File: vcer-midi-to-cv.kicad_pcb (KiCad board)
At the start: 4 copper layers, 210.7 x 128.5 mm, 87 parts, among them J1 Conn_01x10_Male, J10 CV3, J11 CV4, J12 Vel1, J13 Vel2, J14 Vel3, J15 Vel4, J16 Gate1, J17 Gate2, J18 Gate3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

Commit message: I have some changes, but no idea what
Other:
- board size 210.7 x 128.5 mm -> 140 x 100 mm
- board text removed: "!!! TAKE COVER PANEL FROM THE VERSION 4 !!!"
- board text removed: "CV"
- board text removed: "Con"
- board text removed: "Data"
- board text removed: "Gate"
- board text removed: "I"
- board text removed: "II"
- board text removed: "III"
- board text removed: "IV"
- board text removed: "Pwr"
- board text removed: "USB"
- board text removed: "Upgrade"
- board text removed: "Vel"
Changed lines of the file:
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@@
   (gr_circle locked (center 9.01 95.96) (end 9.428688 95.96) (layer "B.SilkS") (width 0.15) (fill solid))
   (gr_circle (center 107.22 66.96) (end 107.638688 66.96) (layer "B.SilkS") (width 0.15) (fill solid))
-  (gr_line (start -79.99 -20.4) (end -9.72 -20.24) (layer "B.SilkS") (width 0.15))
-  (gr_line (start -80.49 119.63) (end -9.56 119.3) (layer "B.SilkS") (width 0.15))
   (gr_circle (center 136.4 23.94) (end 136.818688 23.94) (layer "B.SilkS") (width 0.15) (fill solid))
   (gr_circle (center 124.87 66.36) (end 125.288688 66.36) (layer "B.SilkS") (width 0.15) (fill solid))
-  (gr_line (start -9.72 119.97) (end -79.99 -20.4) (layer "B.SilkS") (width 0.15))
   (gr_circle locked (center 9.02 4.23) (end 9.438688 4.23) (layer "B.SilkS") (width 0.15) (fill solid))
   (gr_circle (center 104.31 51.66) (end 104.728688 51.66) (layer "B.SilkS") (width 0.15) (fill solid))
   (gr_circle (center 137.76 67.79) (end 138.178688 67.79) (layer "B.SilkS") (width 0.15) (fill solid))
-  (gr_line (start -9.72 -20.24) (end -80.49 119.63) (layer "B.SilkS") (width 0.15))
   (gr_circle (center 108 4.211312) (end 108.418688 4.211312) (layer "F.SilkS") (width 0.15) (fill solid))
   (gr_circle (center 115.4 66.08) (end 115.818688 66.08) (layer "F.SilkS") (width 0.15) (fill solid))
@@
   (gr_circle (center 108.68 95.29) (end 109.098688 95.29) (layer "F.SilkS") (width 0.15) (fill solid))
   (gr_circle (center 132.7 66.22) (end 133.118688 66.22) (layer "F.SilkS") (width 0.15) (fill solid))
-  (gr_line (start -20.194086 -14.25) (end -20.194086 114.25) (layer "Edge.Cuts") (width 0.15))
-  (gr_line (start -70.694086 114.25) (end -20.194086 114.25) (layer "Edge.Cuts") (width 0.15))
-  (gr_line (start -70.694086 -14.25) (end -20.194086 -14.25) (layer "Edge.Cuts") (width 0.15))
+  (gr_line locked (start 40 100) (end 40 0) (layer "Edge.Cuts") (width 0.2))
+  (gr_line locked (start 0 100) (end 0 0) (layer "Edge.Cuts") (width 0.2))
+  (gr_line locked (start 0 100) (end 40 100) (layer "Edge.Cuts") (width 0.2))
+  (gr_line locked (start 140 100) (end 140 0) (layer "Edge.Cuts") (width 0.2))
+  (gr_line locked (start 0 0) (end 40 0) (layer "Edge.Cuts") (width 0.2))
+  (gr_line locked (start 100 100) (end 100 0) (layer "Edge.Cuts") (width 0.2))
+  (gr_line locked (start 100 0) (end 140 0) (layer "Edge.Cuts") (width 0.2))
   (gr_line locked (start 100 100) (end 140 100) (layer "Edge.Cuts") (width 0.2))
-  (gr_line locked (start 0 100) (end 0 0) (layer "Edge.Cuts") (width 0.2))
-  (gr_line locked (start 140 100) (end 140 0) (layer "Edge.Cuts") (width 0.2))
-  (gr_line locked (start 0 100) (end 40 100) (layer "Edge.Cuts") (width 0.2))
-  (gr_line locked (start 40 100) (end 40 0) (layer "Edge.Cuts") (width 0.2))
-  (gr_line locked (start 100 0) (end 140 0) (layer "Edge.Cuts") (width 0.2))
-  (gr_line locked (start 0 0) (end 40 0) (layer "Edge.Cuts") (width 0.2))
-  (gr_line (start -70.694086 -14.25) (end -70.694086 114.25) (layer "Edge.Cuts") (width 0.15))
-  (gr_line locked (start 100 100) (end 100 0) (layer "Edge.Cuts") (width 0.2))
-  (gr_line (start -70.694086 -11.25) (end -20.194086 -11.25) (layer "User.8") (width 0.15))
   (gr_line locked (start 140 2.5) (end 100 2.5) (layer "User.8") (width 0.15))
   (gr_line locked (start 102.475 0.05) (end 102.475 100.05) (layer "User.8") (width 0.15))
   (gr_line locked (start 137.475 100.05) (end 137.475 0.05) (layer "User.8") (width 0.15))
-  (gr_line (start -70.694086 111.25) (end -20.194086 111.25) (layer "User.8") (width 0.15))
   (gr_line locked (start 40 99.5) (end 0 99.5) (layer "User.9") (width 0.15))
   (gr_line locked (start 100.5 100) (end 100.5 0) (layer "User.9") (width 0.15))
@@
     (effects (font (size 0.5 0.5) (thickness 0.125)) (justify mirror))
   )
-  (gr_text "III" (at -65.669086 69.775) (layer "F.SilkS")
-    (effects (font (size 2 2) (thickness 0.3)))
-  )
-  (gr_text "Pwr" (at -30.619086 16.2) (layer "F.SilkS")
-    (effects (font (size 1 1) (thickness 0.15)))
-  )
-  (gr_text "Data" (at -36.644086 16.2) (layer "F.SilkS")
-    (effects (font (size 1 1) (thickness 0.15)))
-  )
-  (gr_text "II" (at -65.669086 55.375) (layer "F.SilkS")
-    (effects (font (size 2 2) (thickness 0.3)))
-  )
-  (gr_text "Vel" (at -31.719086 34.525) (layer "F.SilkS")
-    (effects (font (size 2 2) (thickness 0.3)))
-  )
-  (gr_text "IV" (at -65.669086 84.175) (layer "F.SilkS")
-    (effects (font (size 2 2) (thickness 0.3)))
-  )
-  (gr_text "I" (at -65.669086 40.975) (layer "F.SilkS")
-    (effects (font (size 2 2) (thickness 0.3)))
-  )
-  (gr_text "Con" (at -42.819086 16.2) (layer "F.SilkS")
-    (effects (font (size 1 1) (thickness 0.15)))
-  )
   (gr_text "Back Panel" (at 107 3) (layer "F.SilkS")
     (effects (font (size 1 1) (thickness 0.15)))
@@
   (gr_text "Front Panel" (at 7 3) (layer "F.SilkS")
     (effects (font (size 1 1) (thickness 0.15)))
-  )
-  (gr_text "CV" (at -58.369086 34.525) (layer "F.SilkS")
-    (effects (font (size 2 2) (thickness 0.3)))
-  )
-  (gr_text "Gate" (at -45.294086 34.525) (layer "F.SilkS")
-    (effects (font (size 2 2) (thickness 0.3)))
-  )
-  (gr_text "USB" (at -53.744086 12.025) (layer "F.SilkS")
-    (effects (font (size 1 1) (thickness 0.15)))
-  )
-  (gr_text "Upgrade" (at -55.044086 27.775) (layer "F.SilkS")
-    (effects (font (size 1 1) (thickness 0.15)))
-  )
-  (gr_text "!!! TAKE COVER PANEL FROM THE VERSION 4 !!!" (at -44.93 56.53 45) (layer "User.4")
-    (effects (font (size 2 2) (thickness 0.15)))
   )
   (segment locked (start 112.525 30.779289) (end 112.525 29.875) (width 0.25) (layer "F.Cu") (net 1))
@@
     )
   )
-  (group "" (id 0d5502a4-78ea-4afd-9163-5fff06168194)
-    (members
-      0f01468d-4793-40a9-aa18-d4ec9b5eefff
-      30bb5606-9eda-48c1-9bd4-a93423426ac8
-      347abbc1-854a-40f3-be93-e7f380c88c8b
-      40dfc13f-f9a8-4ff3-bcab-1084fdf596c9
-      b5f8a962-6395-475e-a632-f26449ff4189
-      de954fc5-54aa-4912-850f-059c315d7062
-    )
-  )
   (group "" locked (id 3739076a-baeb-4668-95d4-28b7b5f3ab71)
     (members
@@
     )
   )
-  (group "" (id d4f87279-b883-4cb1-a4a4-84fef4bb4711)
-    (members
-      067063ef-affc-4d22-8463-eb3e4abccdc8
-      0d5502a4-78ea-4afd-9163-5fff06168194
-      2105cf5c-9eed-41f6-a88b-9d9562cde9a4
-      266e3bba-095d-4c7e-a334-d2acc8c5dfc8
-      34eb0245-4c12-4186-b799-98f2fe22efa8
-      3d3b04f2-b9f9-43bb-8d5b-593d5fcc3cf6
-      4c12a19f-f97f-45c8-8cfd-4d705aa2b9e7
-      51a33ff5-e59d-449b-875a-042da405201c
-      575d4f8c-99b7-4588-a1dd-31e4d0008428
-      94325249-10dc-49aa-b4bc-3f8b4aee802f
-      9b229dce-e01f-436d-aa19-067b1fc2c250
-      c69a4a08-fb84-4571-9982-802ea557f9b2
-      d39554fa-e09b-403f-be3b-055b6f2061d2
-    )
-  )

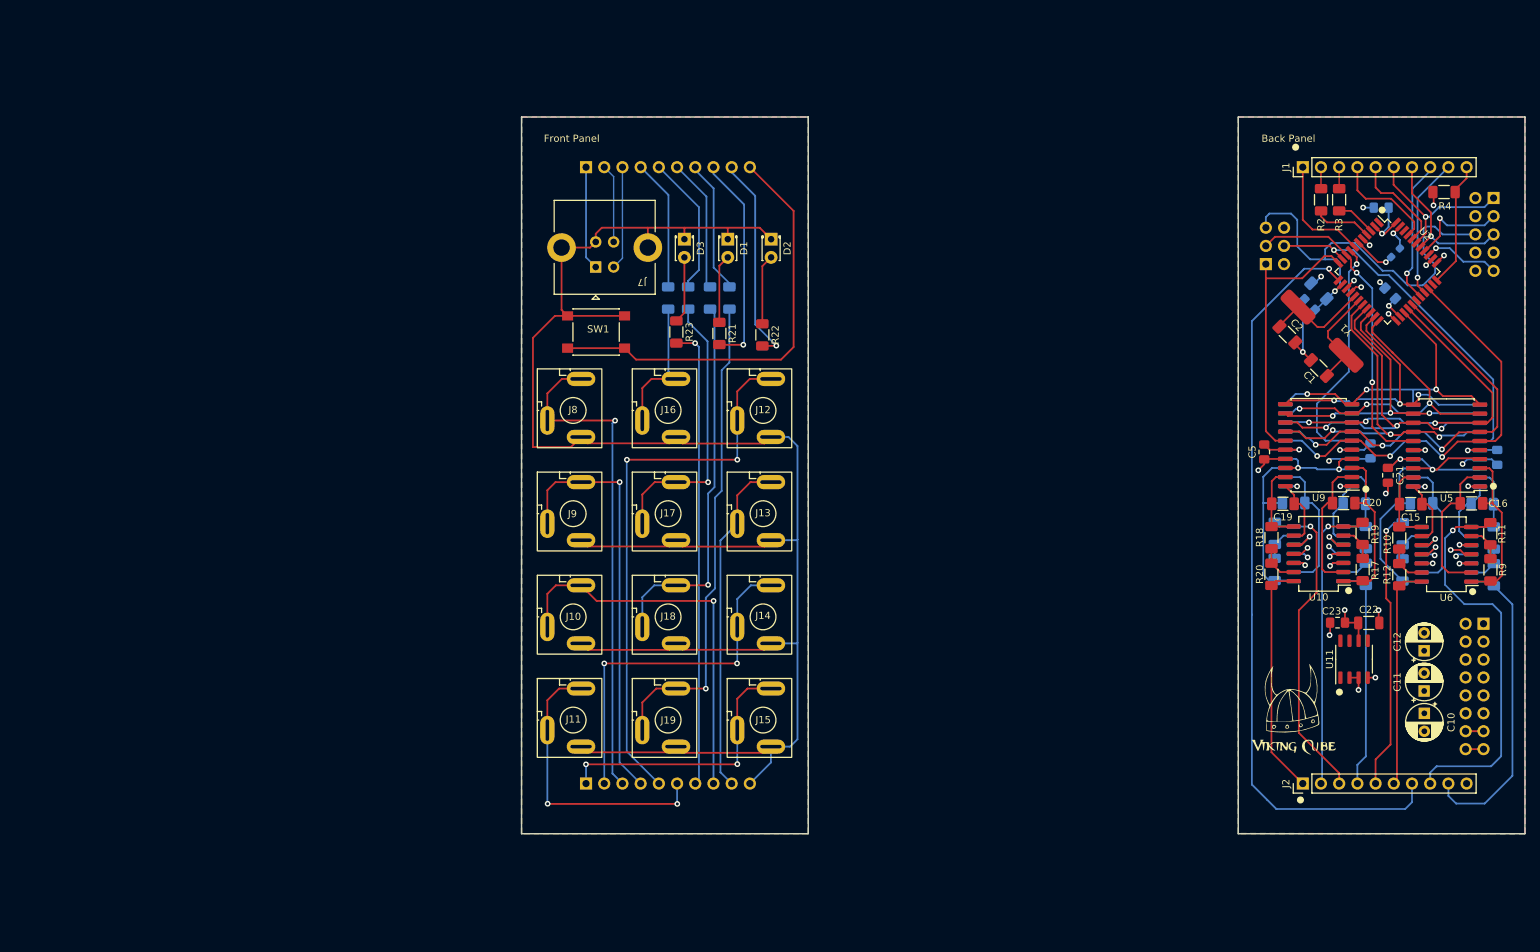
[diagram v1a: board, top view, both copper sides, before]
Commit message: recovered the cover plate from the old version - I declare v2.0 here by
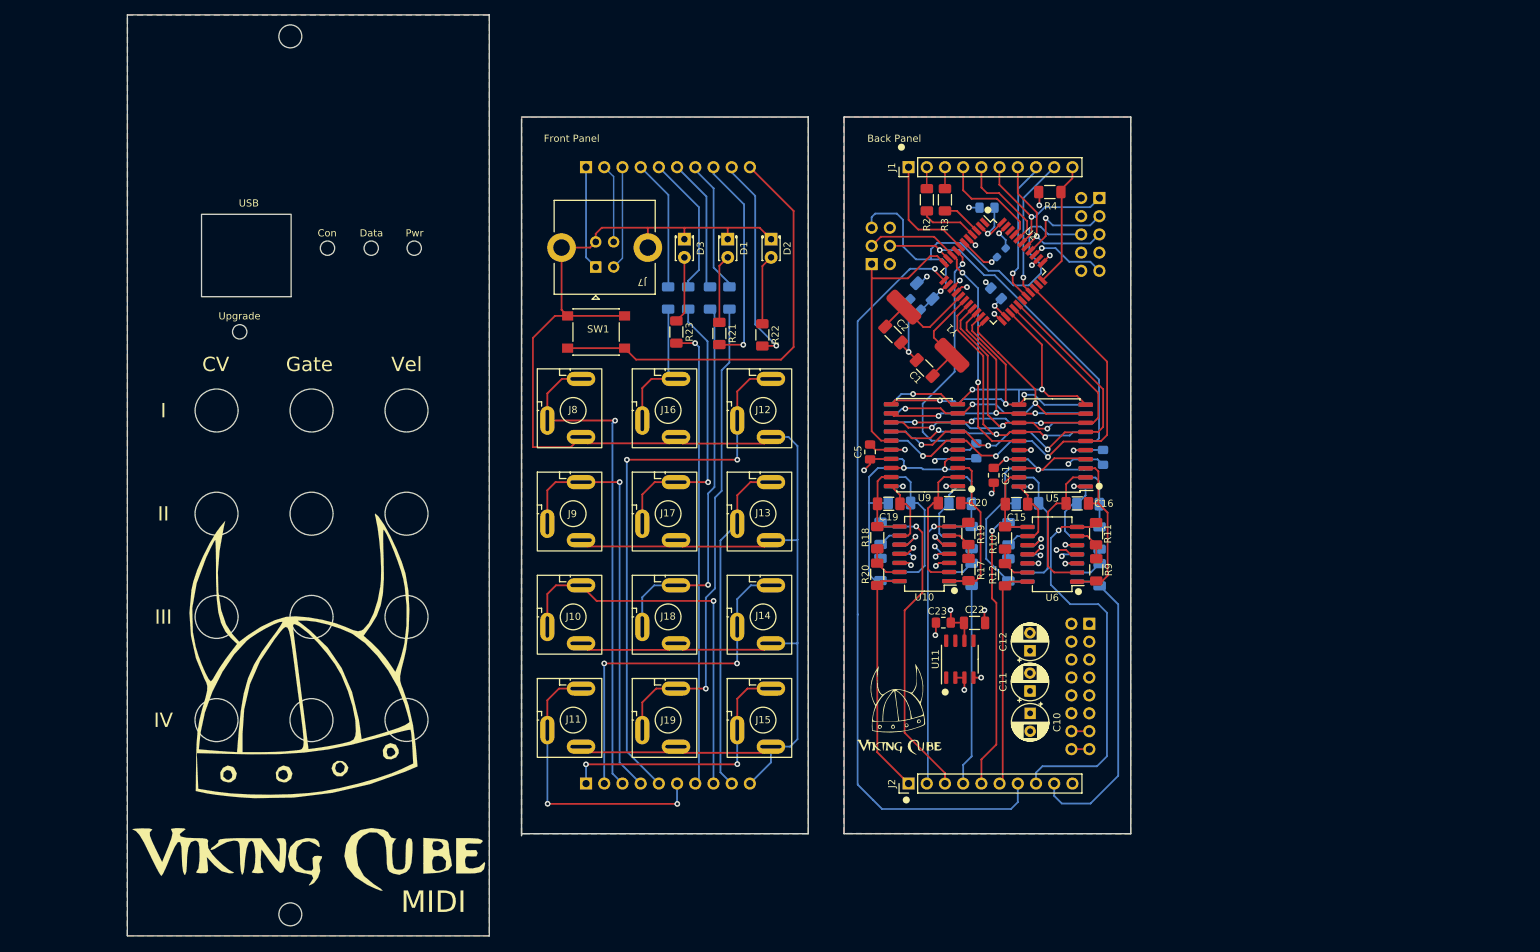
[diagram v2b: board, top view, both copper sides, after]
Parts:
- added G***: LOGO, eurorack:logo2, F.Cu at (-19.9, 89.7)
- added REF**: mount_m3_hole, eurorack:mount_m3_hole, F.Cu at (-29.8, -11.2)
- added REF1: mount_LUM_1502-03, eurorack:mount_LUM_1502-03, F.Cu at (-16.1, 84.1)
- added REF10: mount_LUM_1502-03, eurorack:mount_LUM_1502-03, F.Cu at (-16.1, 41.0)
- added REF11: mount_LUM_1502-03, eurorack:mount_LUM_1502-03, F.Cu at (-29.3, 41.0)
- added REF12: mount_LUM_1502-03, eurorack:mount_LUM_1502-03, F.Cu at (-42.5, 41.0)
- added REF13: mount_m2, eurorack:mount_m2, F.Cu at (-39.3, 30.0)
- added REF14: mount_m2, eurorack:mount_m2, F.Cu at (-21.0, 18.3)
- added REF15: mount_m2, eurorack:mount_m2, F.Cu at (-15.0, 18.3)
- added REF16: mount_m2, eurorack:mount_m2, F.Cu at (-27.1, 18.3)
- added REF17: mount_USB-BG, eurorack:mount_USB-BG, F.Cu at (-32.4, 18.4)
- added REF2: mount_LUM_1502-03, eurorack:mount_LUM_1502-03, F.Cu at (-29.3, 84.2)
- added REF3: mount_LUM_1502-03, eurorack:mount_LUM_1502-03, F.Cu at (-42.6, 84.2)
- added REF4: mount_LUM_1502-03, eurorack:mount_LUM_1502-03, F.Cu at (-16.1, 69.8)
- added REF5: mount_LUM_1502-03, eurorack:mount_LUM_1502-03, F.Cu at (-29.3, 69.8)
- added REF6: mount_LUM_1502-03, eurorack:mount_LUM_1502-03, F.Cu at (-42.5, 69.8)
- added REF7: mount_LUM_1502-03, eurorack:mount_LUM_1502-03, F.Cu at (-16.1, 55.4)
- added REF8: mount_LUM_1502-03, eurorack:mount_LUM_1502-03, F.Cu at (-29.3, 55.4)
- added REF9: mount_LUM_1502-03, eurorack:mount_LUM_1502-03, F.Cu at (-42.6, 55.4)
- moved C17 55.0 mm to (79.0, 54.0)
- moved R14 55.0 mm to (80.6, 58.7)
- moved R4 55.0 mm to (73.7, 10.5)
- moved U7 55.0 mm to (74.0, 45.9)
- moved G*** 55.0 mm to (55.0, 84.6)
- moved R18 55.0 mm to (49.6, 58.7)
- moved U3 55.0 mm to (56.2, 45.8)
- moved Y1 55.0 mm to (60.1, 33.2)
- moved C1 55.0 mm to (56.2, 35.0)
- moved C10 55.0 mm to (71.0, 83.2)
- moved C11 55.0 mm to (70.9, 80.1)
- moved C12 55.0 mm to (70.9, 74.5)
- moved C13 55.0 mm to (61.2, 54.0)
- moved C15 55.0 mm to (69.1, 54.0)
- moved C16 55.0 mm to (77.5, 53.9)
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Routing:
- added copper zone on B.Cu, net (none)
- added copper zone on F.Cu, net (none)
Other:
- board size 140 x 100 mm -> 140 x 128.5 mm
- board text added: "+45;0"
- board text added: "-55;0 [-50] 10HP"
- board text added: "CV"
- board text added: "Con"
- board text added: "Data"
- board text added: "Gate"
- board text added: "I"
- board text added: "II"
- board text added: "III"
- board text added: "IV"
- board text added: "JLCJLCJLCJLC"
- board text added: "MIDI"
- board text added: "Pwr"
- board text added: "USB"
- board text added: "Upgrade"
- board text added: "Vel"
